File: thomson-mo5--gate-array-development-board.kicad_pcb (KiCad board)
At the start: 2 copper layers, 99.7 x 99.7 mm, 17 parts, among them J1 JTAG, J2 VPP connector, J3 5V->12V, J4 Adjustable MT3608 module, U1 4040, U2 4040, U3 GATE_ARRAY_MO5_V1_SOCKET, U4 GATE_ARRAY_MO5_V2_SOCKET, X1 XO 16MHz - DIP 8 or 14

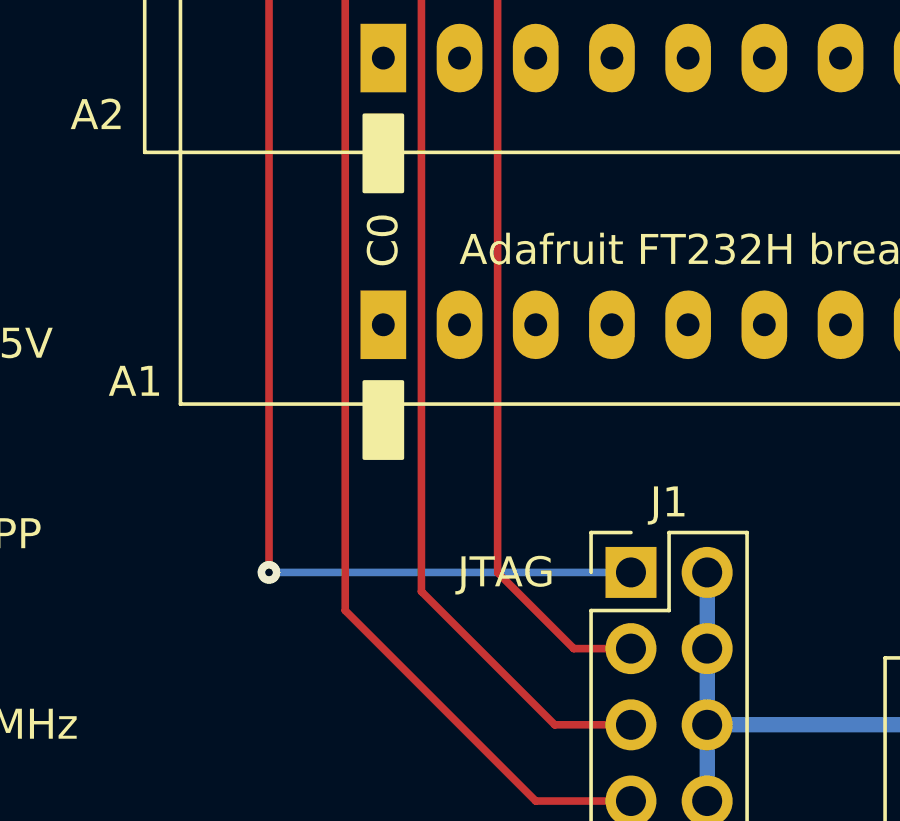
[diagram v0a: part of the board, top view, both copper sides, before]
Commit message: completed copper pour
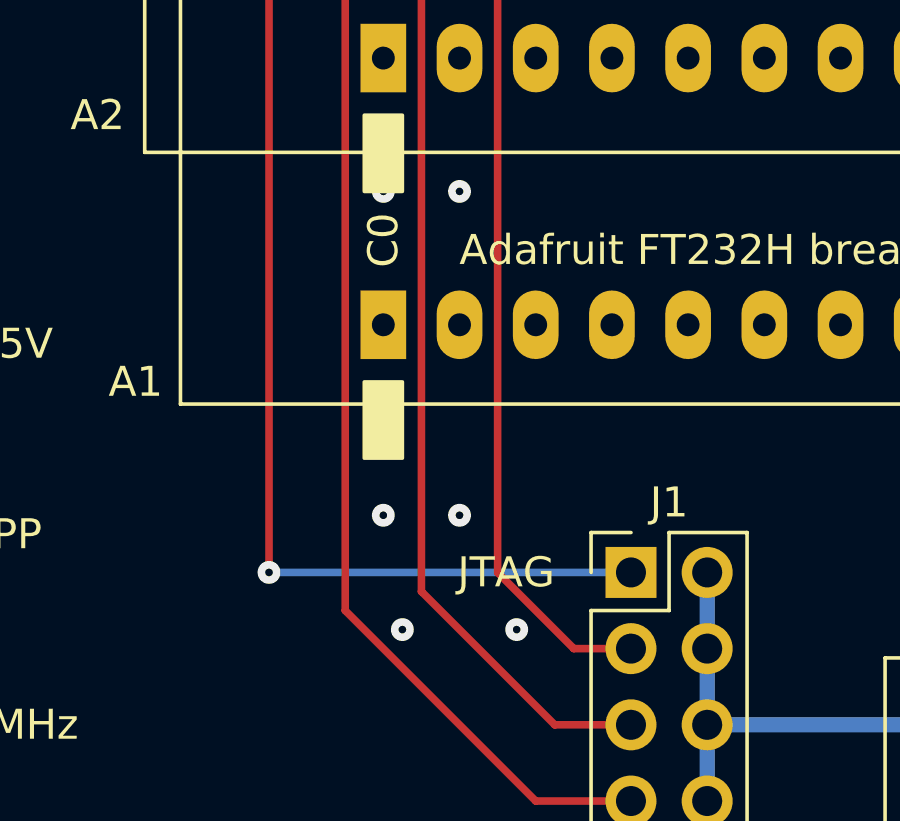
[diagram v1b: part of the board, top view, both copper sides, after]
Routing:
- net GND: vias 0 -> 6
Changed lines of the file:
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@@
     (effects (font (size 1 1) (thickness 0.1)) (justify left))
   )
+  (via (at 112.395 120.015) (size 0.762) (drill 0.254) (layers "F.Cu" "B.Cu") (free) (net 11))
+  (via (at 116.84 123.825) (size 0.762) (drill 0.254) (layers "F.Cu" "B.Cu") (free) (net 11))
+  (via (at 114.935 109.22) (size 0.762) (drill 0.254) (layers "F.Cu" "B.Cu") (free) (net 11))
+  (via (at 113.03 123.825) (size 0.762) (drill 0.254) (layers "F.Cu" "B.Cu") (free) (net 11))
+  (via (at 112.395 109.22) (size 0.762) (drill 0.254) (layers "F.Cu" "B.Cu") (free) (net 11))
+  (via (at 114.935 120.015) (size 0.762) (drill 0.254) (layers "F.Cu" "B.Cu") (free) (net 11))
   (segment (start 137.16 76.835) (end 137.795 77.47) (width 0.508) (layer "B.Cu") (net 11))
   (segment (start 132.715 95.885) (end 137.795 100.965) (width 0.508) (layer "B.Cu") (net 11))

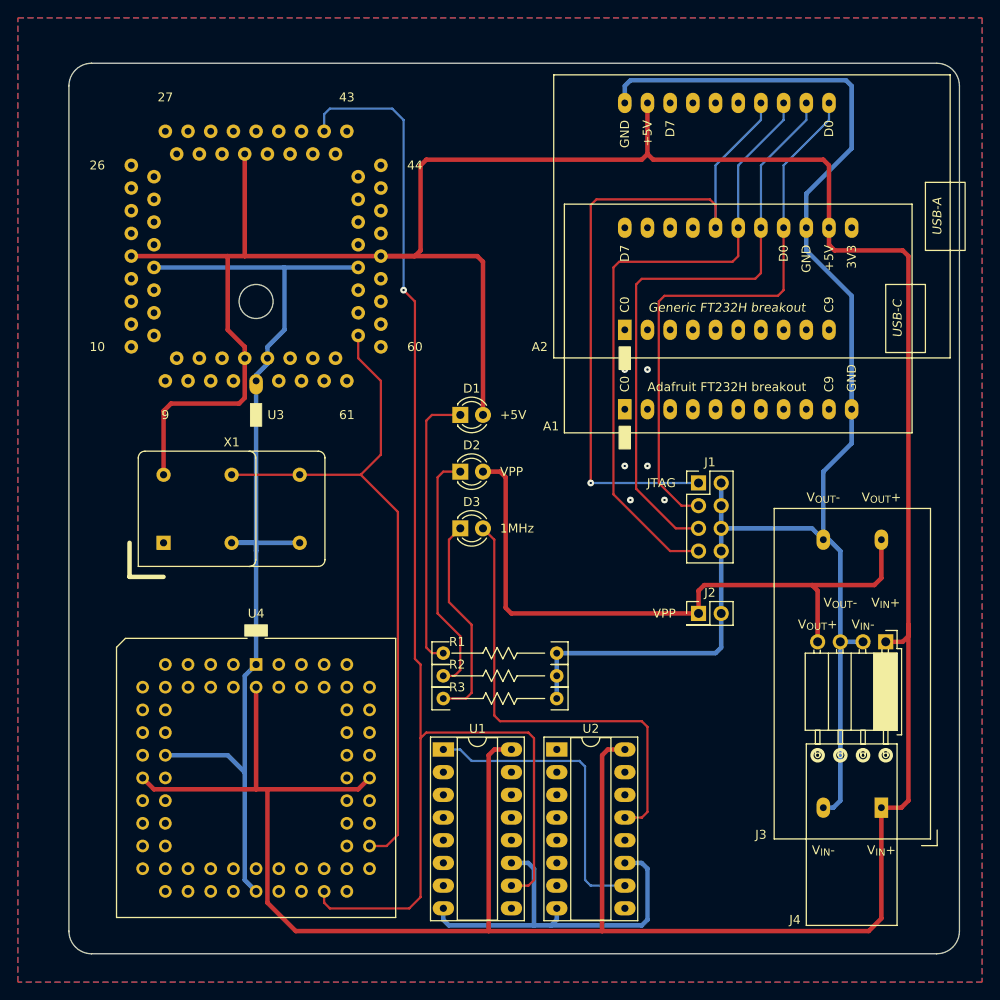
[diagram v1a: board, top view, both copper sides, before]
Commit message: Labeled the PCB, commited the footprints
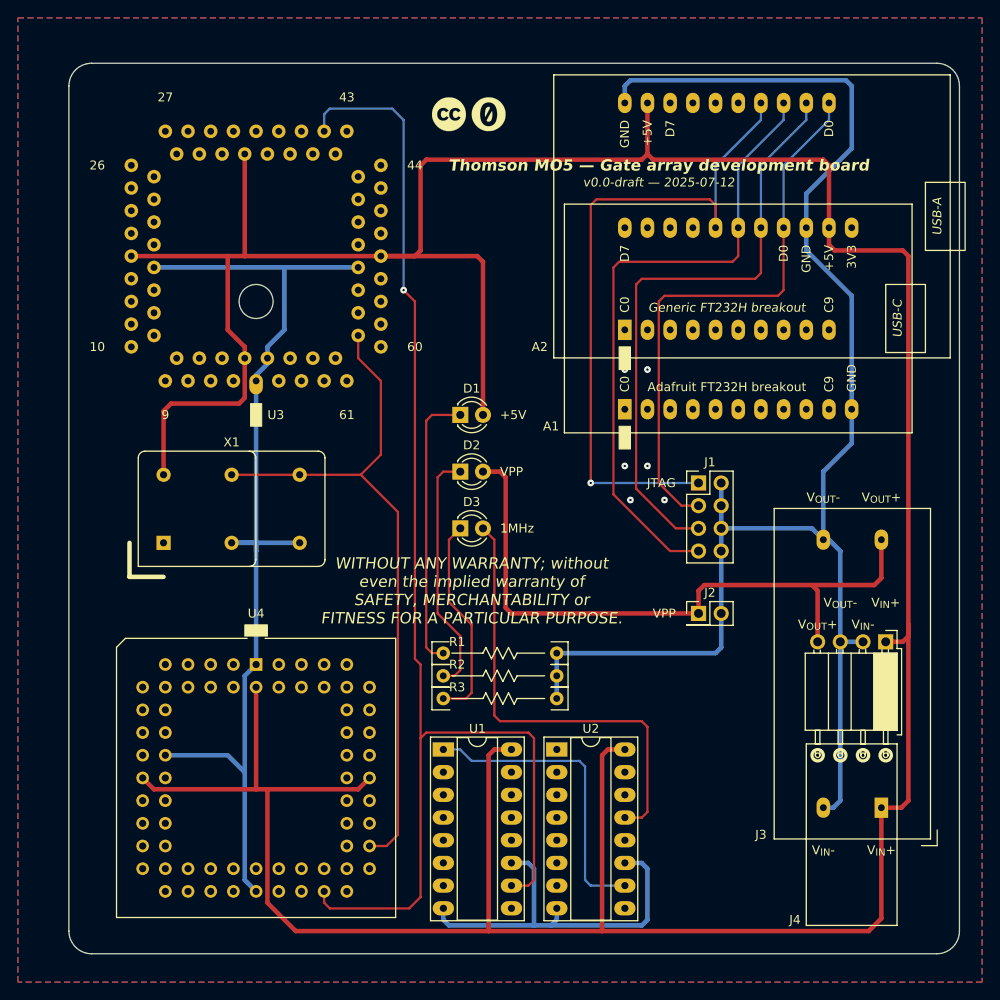
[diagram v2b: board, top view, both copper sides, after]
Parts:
- added G***: LOGO, cliparts:logo--cc--cc, F.Cu at (92.7, 80.6)
- added G***: LOGO, cliparts:logo--cc--zero, F.Cu at (97.2, 80.6)
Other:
- board text added: "${REVISION} — ${ISSUE_DATE}"
- board text added: "${TITLE}"
- board text added: "WITHOUT ANY WARRANTY; without even the implied warranty of SAFETY, MERCHANTABILITY or FITNESS FOR A PARTICULAR PURPOSE."
